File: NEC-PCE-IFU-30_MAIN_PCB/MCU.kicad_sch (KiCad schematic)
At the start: 39 parts, among them CN10 Conn_02x02_Odd_Even, CN6 Conn_02x02_Odd_Even, CN7 Conn_02x08_Odd_Even, CN8 Conn_02x04_Odd_Even, CN9 Conn_02x05_Odd_Even, IC110 CXK5816, IC112 M41464, IC113 M41464, IC130 D91061GD, IC132 74HC245, IC133 74HC245

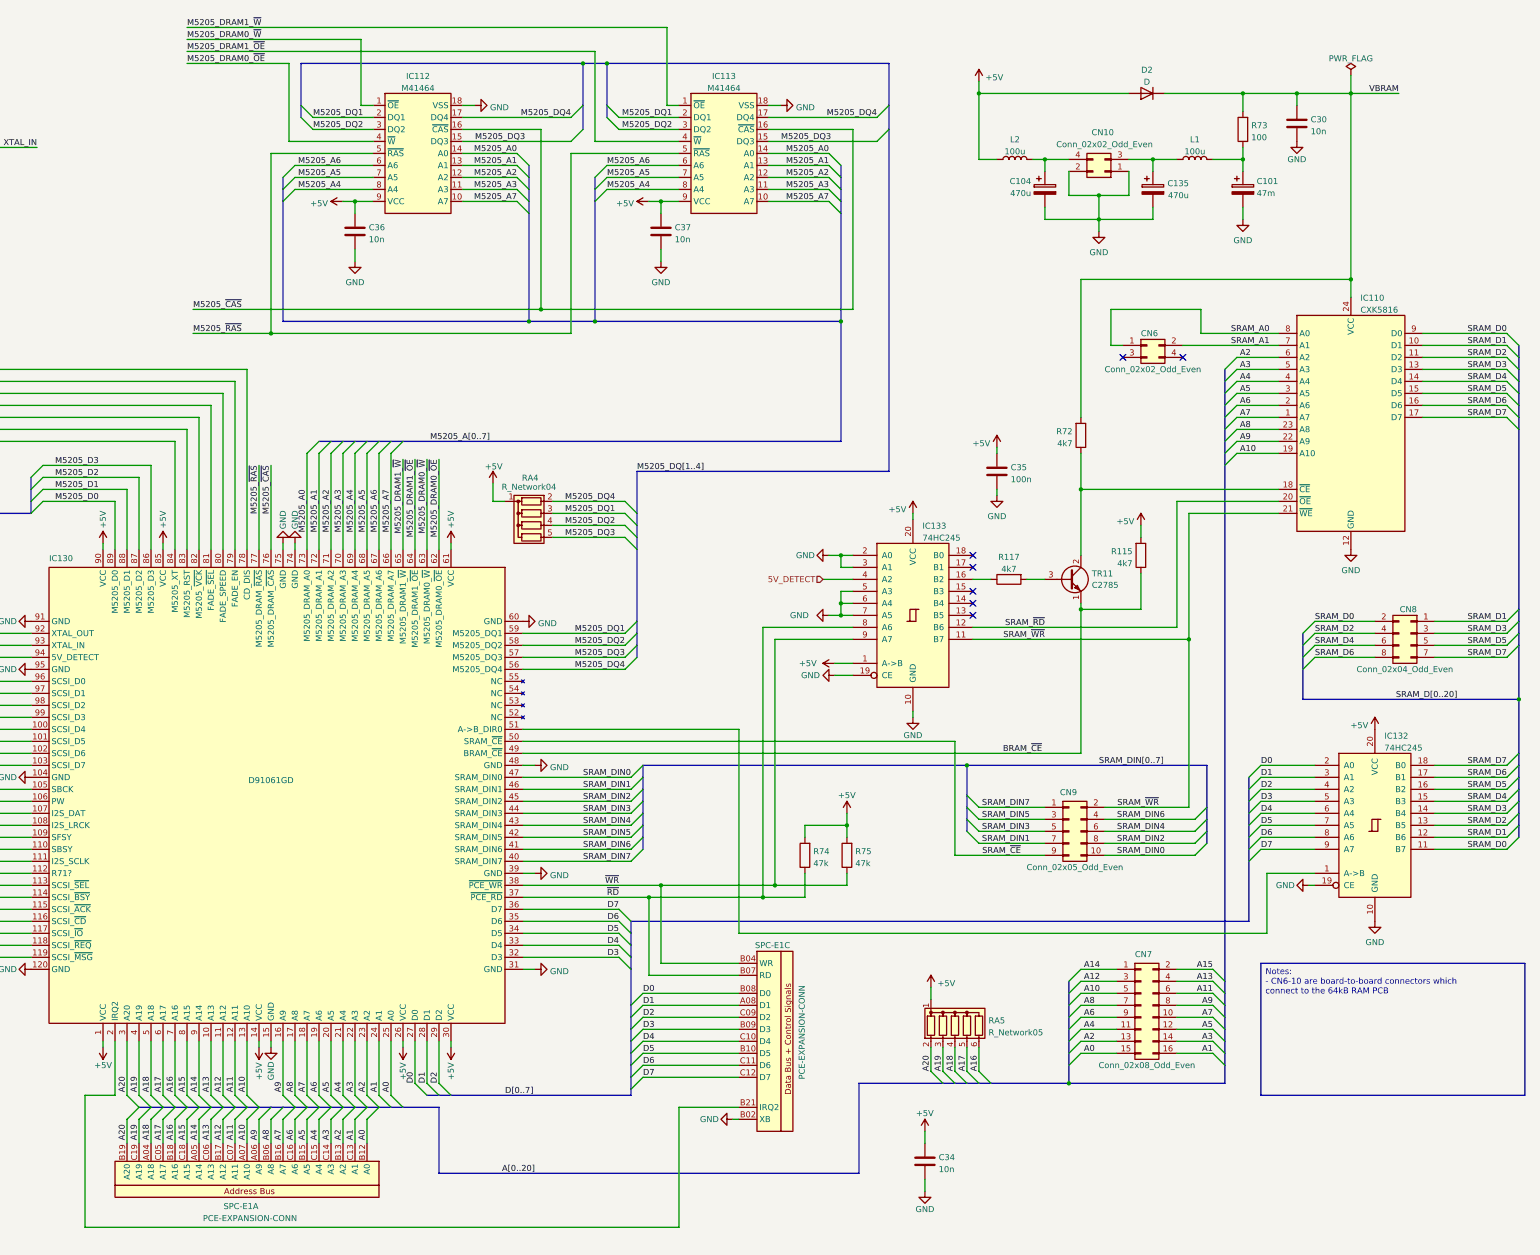
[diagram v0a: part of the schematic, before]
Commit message: Fixed a lot of issues on data bus on the MCU page.
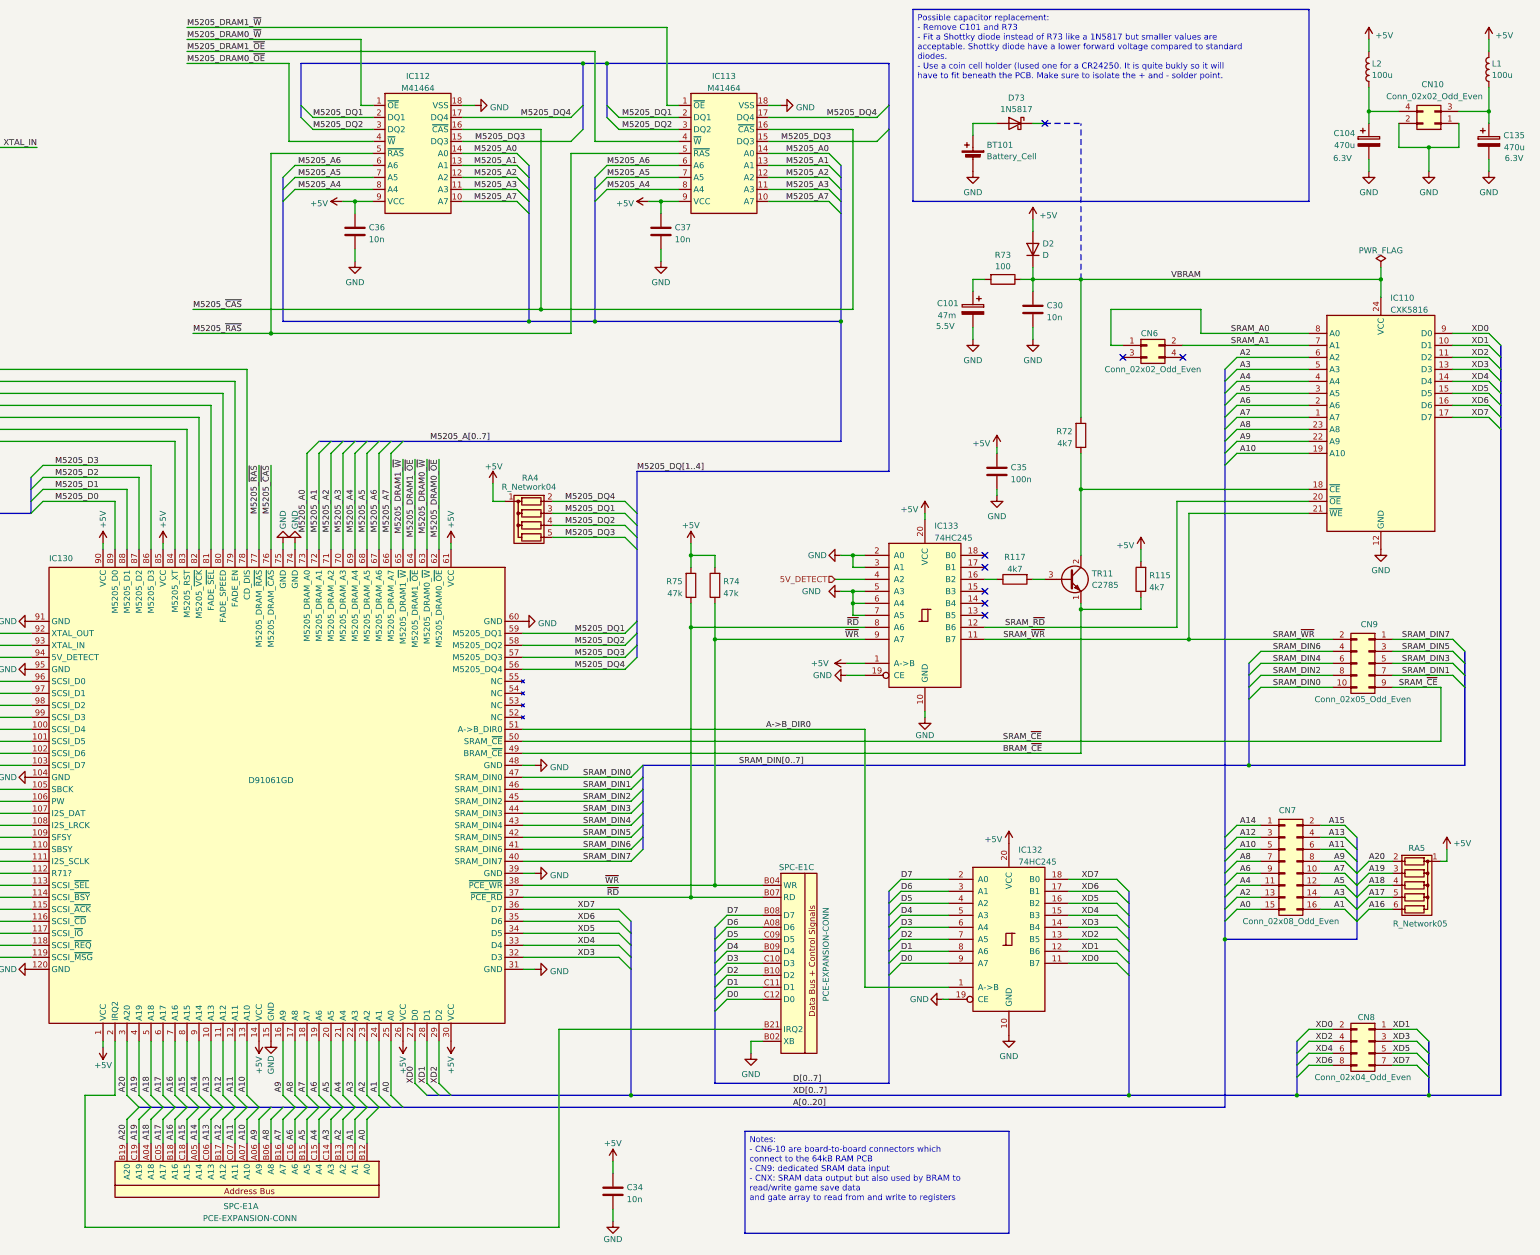
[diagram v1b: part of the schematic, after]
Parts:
- added BT101: Battery_Cell, symbol Device:Battery_Cell
- added D73: 1N5817, Diode_THT:D_DO-41_SOD81_P10.16mm_Horizontal, symbol Diode:1N5817
- C101: Voltage (none) -> 5.5V
- C104, C135: Voltage (none) -> 6.3V
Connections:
- net +5V: now also L1.1, L2.1; no longer L2.2
- net D0: now also IC132.9 (A7), SPC-E1.C12 (D0); no longer IC130.27 (D0), IC132.2 (A0), SPC-E1.B08 (D0)
- net D1: now also IC132.8 (A6), SPC-E1.C11 (D1); no longer IC130.28 (D1), IC132.3 (A1), SPC-E1.A08 (D1)
- net D2: now also IC132.7 (A5), SPC-E1.B10 (D2); no longer IC130.29 (D2), IC132.4 (A2), SPC-E1.C09 (D2)
- net D3: now also IC132.6 (A4), SPC-E1.C10 (D3); no longer IC130.32 (D3), IC132.5 (A3), SPC-E1.B09 (D3)
- net D4: now also IC132.5 (A3), SPC-E1.B09 (D4); no longer IC130.33 (D4), IC132.6 (A4), SPC-E1.C10 (D4)
- net D5: now also IC132.4 (A2), SPC-E1.C09 (D5); no longer IC130.34 (D5), IC132.7 (A5), SPC-E1.B10 (D5)
- net D6: now also IC132.3 (A1), SPC-E1.A08 (D6); no longer IC130.35 (D6), IC132.8 (A6), SPC-E1.C11 (D6)
- net D7: now also IC132.2 (A0), SPC-E1.B08 (D7); no longer IC130.36 (D7), IC132.9 (A7), SPC-E1.C12 (D7)
- net GND: now also BT101.2 (-)
- net VBRAM: now also R73.1; no longer R73.2
- net ~{RD}: now also R75.1; no longer R74.1
- net ~{WR}: now also R74.1; no longer R75.1
- net A->B_DIR0: now reaches IC130.51 (A->B_DIR0), IC132.1 (A->B)
- net at C104.1, CN10.4 (Pin_4): now also L2.2; no longer L2.1
- net SRAM_D0 renamed XD0
- net XD0: now also IC130.27 (D0)
- net SRAM_D1 renamed XD1
- net XD1: now also IC130.28 (D1)
- net SRAM_D2 renamed XD2
- net XD2: now also IC130.29 (D2)
- net SRAM_D3 renamed XD3
- net XD3: now also IC130.32 (D3)
- net SRAM_D4 renamed XD4
- net XD4: now also IC130.33 (D4)
- net SRAM_D5 renamed XD5
- net XD5: now also IC130.34 (D5)
- net SRAM_D6 renamed XD6
- net XD6: now also IC130.35 (D6)
- net SRAM_D7 renamed XD7
- net XD7: now also IC130.36 (D7)
- new net: BT101.1 (+), D73.2 (A)
- new net: C101.1, R73.2
- no-connect marks 7 -> 8
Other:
- moved on the sheet: C101, C104, C135, C30, C34, CN10, CN7, CN8, CN9, D2, IC110, IC132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
